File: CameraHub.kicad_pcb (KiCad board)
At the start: 4 copper layers, 90.2 x 95.9 mm, 121 parts, among them J1 200528-0100, J10 TE_282834-4, J2 Header 01x04 0.1", J3 Header 01x04 0.1", J4 USB_C_Receptacle_USB2.0_16P, J5 USB_C_Receptacle_USB2.0_16P, J6 Header 01x04 0.1", J7 USB_C_Receptacle_USB2.0_16P, J8 USB_C_Receptacle_USB2.0_16P, J9 Header 01x04 0.1", U1 USBLC6-2P6, U10 USB2514B-I/M2, U11 MIC2026-1xM, U12 MIC2026-1xM, U14 TLV76733QWDRBxQ1, U2 USBLC6-2P6, U3 USBLC6-2P6, U4 USB2514B-I/M2, U5 MIC2026-1xM, U6 MIC2026-1xM, U7 USBLC6-2P6, U8 USBLC6-2P6, U9 USBLC6-2P6, Y1 24MHz, Y2 24MHz

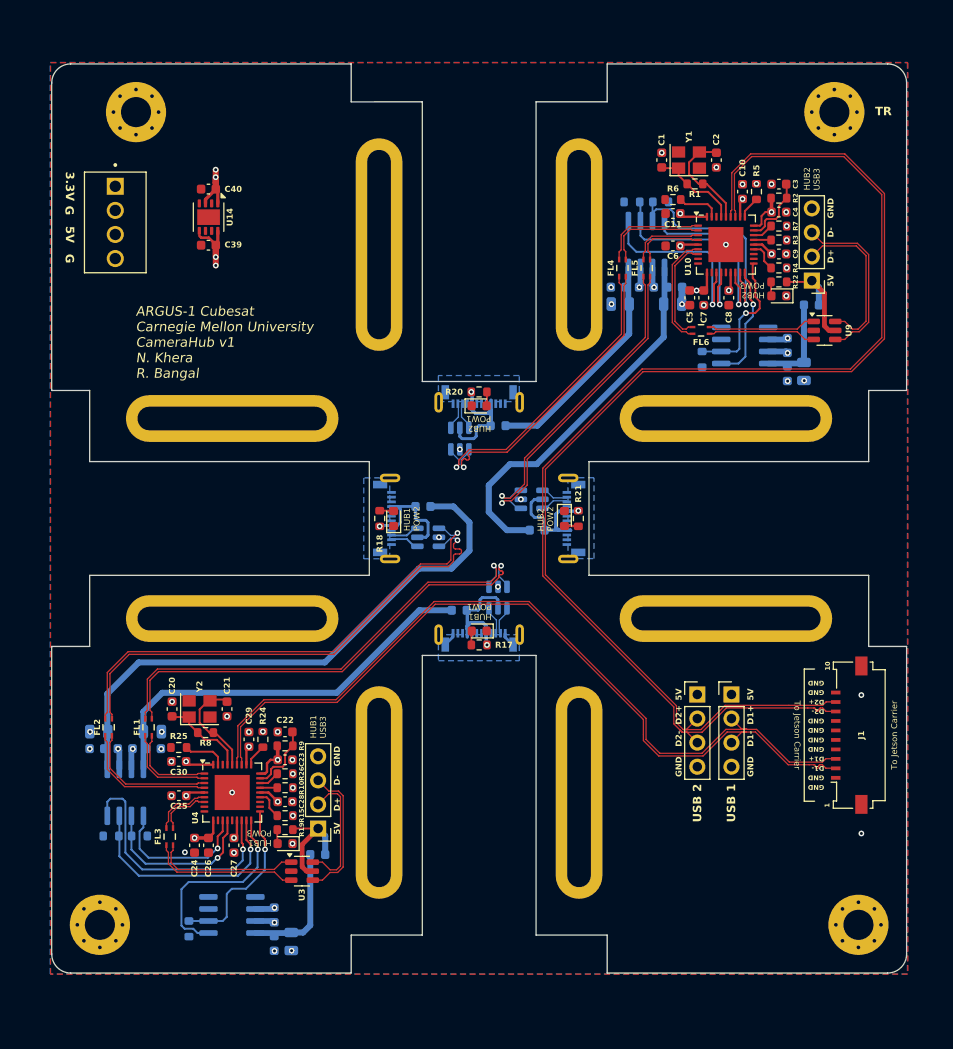
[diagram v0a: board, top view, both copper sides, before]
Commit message: Updated for single USB line
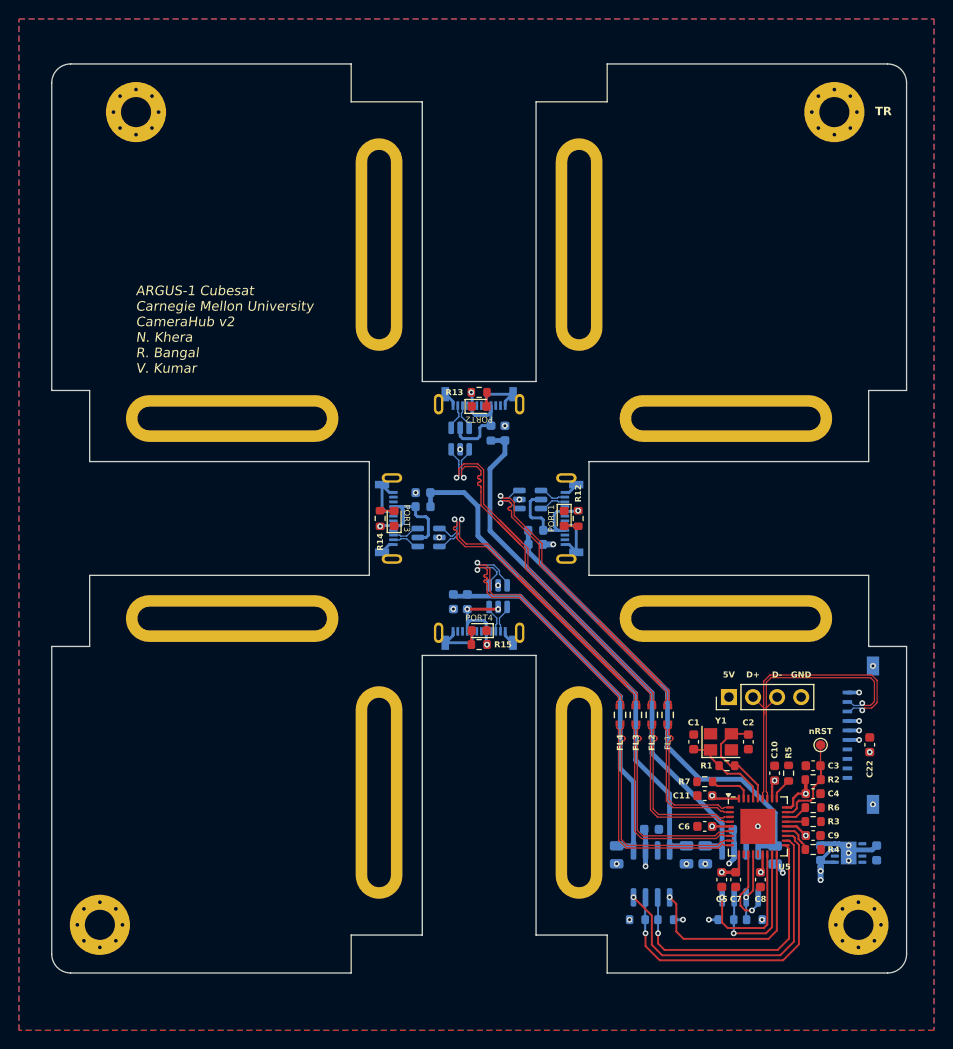
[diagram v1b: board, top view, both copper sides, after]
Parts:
- removed the C20 at (116.5, 116.9)
- removed the C21 at (122.3, 116.9)
- removed the C23 at (128.4, 122.3)
- removed the C24 at (118.9, 131.3)
- removed C25, C26, C27, C28, C29, C30, C31, C33, C35, C36, C38: 0.1uF, Capacitor_SMD:C_0603_1608Metric
- removed C32, C34, C37: 100uF, Capacitor_SMD:C_0805_2012Metric
- removed the D1 at (148.9, 108.7)
- removed the D2 at (139.9, 96.8)
- removed the D3 at (128.4, 131.1)
- removed the FB1 at (146.8, 106.5)
- removed FB6: 600R, Inductor_SMD:L_0603_1608Metric
- removed FL5, FL6: 744230900, CameraHub:CHIP_230900_WRE
- removed the J1 at (187.4, 119.7)
- removed J10: TE_282834-4, CameraHub:TE_282834-4
- removed the J2 at (175.5, 115.4)
- removed the J5 at (139.7, 96.8)
- removed J9: Header 01x04 0.1", Connector_PinHeader_2.54mm:PinHeader_1x04_P2.54mm_Vertical
- removed the R10 at (128.4, 125.2)
- removed R17, R18, R19: 330R, Resistor_SMD:R_0603_1608Metric
- removed R24, R26: 36K, Resistor_SMD:R_0603_1608Metric
- removed R25: 12K, Resistor_SMD:R_0603_1608Metric
- removed R30, R31, R33: 10K, Resistor_SMD:R_0603_1608Metric
- removed the R8 at (120.0, 119.4)
- removed the R9 at (128.4, 120.8)
- removed the U1 at (150.9, 105.2)
- removed the U2 at (143.5, 98.8)
- removed the U3 at (130.2, 134.0)
- removed the U5 at (111.6, 125.7)
- removed the U6 at (122.8, 138.7)
- removed Y2: 24MHz, Crystal:Crystal_SMD_3225-4Pin_3.2x2.5mm
- added C18: 100uF, Capacitor_SMD:C_0805_2012Metric, B.Cu at (163.4, 132.3)
- added C19: 0.1uF, Capacitor_SMD:C_0603_1608Metric, B.Cu at (146.2, 105.6)
- added D4: Green, LED_SMD:LED_0603_1608Metric, F.Cu at (148.9, 108.7)
- added J3: USB_C_Receptacle_USB2.0_16P, CameraHub:USBC-121SMT-4BS2S, B.Cu at (139.9, 96.8)
- added R11: 10K, Resistor_SMD:R_0603_1608Metric, B.Cu at (165.6, 139.1)
- added nRST: Conn_01x01, TestPoint:TestPoint_Pad_D1.0mm, F.Cu at (184.9, 120.7)
- C22: value 0.1uF -> 1uF
- C23: renamed from C39; moved to B.Cu
- C24: renamed from C40; moved to B.Cu
- J6: value Header 01x04 0.1" -> 200528-0100; footprint Connector_PinHeader_2.54mm:PinHeader_1x04_P2.54mm_Vertical -> Connector_FFC-FPC:Molex_200528-0100_1x10-1MP_P1.00mm_Horizontal; moved to B.Cu
- R15: value 36K -> 330R
- U3: renamed from U9; moved to B.Cu
- U4: value USB2514B-I/M2 -> USBLC6-2P6; footprint Package_DFN_QFN:QFN-36-1EP_6x6mm_P0.5mm_EP3.7x3.7mm -> Package_TO_SOT_SMD:SOT-23-6; moved to B.Cu
- U8: renamed from U14; moved to B.Cu
- moved C23 95.3 mm to (190.8, 132.1), turned to 90 degrees
- moved C24 95.2 mm to (184.9, 132.1), turned to 90 degrees
- moved U8 95.2 mm to (187.9, 132.1), turned to 0 degrees
- moved R8 76.8 mm to (177.9, 139.1), turned to 180 degrees
- moved R9 76.0 mm to (174.9, 139.1), turned to 0 degrees
- moved U6 67.1 mm to (176.4, 134.3), turned to 90 degrees
- moved C22 61.7 mm to (190.1, 120.7), turned to -90 degrees
- moved R7 61.5 mm to (172.7, 124.6)
- moved C11 61.5 mm to (172.7, 126.1)
- moved U5 61.5 mm to (178.3, 129.3)
- moved C1 61.5 mm to (171.5, 120.4)
- moved C2 61.5 mm to (177.3, 120.4)
- moved C5 61.5 mm to (174.5, 134.9)
- moved C7 61.5 mm to (176.0, 134.9)
- moved R1 61.5 mm to (175.0, 122.9)
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- renumbered C18 to C20, C19 to C21, D4 to D1, D5 to D2, D6 to D3, FB2 to FB1, FB5 to FB2, J7 to J1, J8 to J2, J3 to J5, R16 to R10, R20 to R12, R21 to R13, R22 to R14, R7 to R6, R6 to R7, R11 to R8, R12 to R9, U7 to U1, U8 to U2, U10 to U5, U11 to U6, U12 to U7
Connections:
- net /nRST2 renamed /nRST
- C22 pad 1: /nRST1 -> GND
- C22 pad 2: GND -> +5V
- FB3 pad 1: /Hub 1/VBUS3 -> /Hub 2/VBUS3
- FB3 pad 2: /Hub 1/VBUS_CONN3 -> /Hub 2/VBUS_CONN3
- FB4 pad 1: /Hub 1/VBUS2 -> /Hub 2/VBUS4
- FB4 pad 2: /Hub 1/VBUS_CONN2 -> /Hub 2/VBUS_CONN4
- FL1 pad 1: /Hub 1/HD1_P -> /Hub 2/HD1_P
- FL1 pad 2: /Hub 1/FD1_P -> /Hub 2/FD1_P
- FL1 pad 3: /Hub 1/FD1_N -> /Hub 2/FD1_N
- FL1 pad 4: /Hub 1/HD1_N -> /Hub 2/HD1_N
- FL2 pad 1: /Hub 1/HD2_P -> /Hub 2/HD2_P
- FL2 pad 2: /Hub 1/FD2_P -> /Hub 2/FD2_P
- FL2 pad 3: /Hub 1/FD2_N -> /Hub 2/FD2_N
- FL2 pad 4: /Hub 1/HD2_N -> /Hub 2/HD2_N
- FL3 pad 1: /Hub 1/HD3_P -> /Hub 2/HD3_P
- FL3 pad 2: /Hub 1/FD3_P -> /Hub 2/FD3_P
- FL3 pad 3: /Hub 1/FD3_N -> /Hub 2/FD3_N
- FL3 pad 4: /Hub 1/HD3_N -> /Hub 2/HD3_N
- FL4 pad 1: /Hub 2/HD1_P -> /Hub 2/HD4_P
- FL4 pad 2: /Hub 2/FD1_P -> /Hub 2/FD4_P
- FL4 pad 3: /Hub 2/FD1_N -> /Hub 2/FD4_N
- FL4 pad 4: /Hub 2/HD1_N -> /Hub 2/HD4_N
- J4 pad A4: /Hub 1/VBUS_CONN1 -> /Hub 2/VBUS_CONN4
- J4 pad A6: /Hub 1/D1_P -> /Hub 2/D4_P
- J4 pad A7: /Hub 1/D1_N -> /Hub 2/D4_N
- J4 pad B9: /Hub 1/VBUS_CONN1 -> /Hub 2/VBUS_CONN4
- J5 pad 2: /USB2_P -> /USB_P
- J5 pad 3: /USB2_N -> /USB_N
- J6 pad 1: /Hub 1/VBUS_CONN3 -> GND
- J6 pad 2: /Hub 1/D3_P -> /USB_N
- J6 pad 3: /Hub 1/D3_N -> /USB_P
- R15 pad 1: Net-(U4-SDA/SMBDATA/NON_REM1) -> /Hub 2/VBUS_CONN4
- R15 pad 2: GND -> Net-(D4-A)
- U4 pad 1: /Hub 1/HD1_N -> /Hub 2/FD4_P
- U4 pad 2: /Hub 1/HD1_P -> GND
- U4 pad 3: /Hub 1/HD2_N -> /Hub 2/FD4_N
- U4 pad 4: /Hub 1/HD2_P -> /Hub 2/D4_N
- U4 pad 5: +3.3V -> /Hub 2/VBUS_CONN4
- U4 pad 6: /Hub 1/HD3_N -> /Hub 2/D4_P
- U5 pad 20: unconnected-(U10-PRTPWR4/BC_EN4-Pad20) -> /Hub 2/PWR4
- U5 pad 21: unconnected-(U10-OCS_N4-Pad21) -> /Hub 2/nOCS4
- U5 pad 30: /USB2_N -> /USB_N
- U5 pad 31: /USB2_P -> /USB_P
- U5 pad 8: unconnected-(U10-USBDM_DN4/PRT_DIS_M4-Pad8) -> /Hub 2/HD4_N
- U5 pad 9: unconnected-(U10-USBDP_DN4/PRT_DIS_P4-Pad9) -> /Hub 2/HD4_P
- U7 pad 3: unconnected-(U12-FLGB-Pad3) -> /Hub 2/nOCS4
- U7 pad 4: unconnected-(U12-ENB-Pad4) -> /Hub 2/PWR4
- U7 pad 5: unconnected-(U12-OUTB-Pad5) -> /Hub 2/VBUS4
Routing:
- net /USB2_N: track 133.7 -> 0.00 mm
- net /USB2_P: track 132.7 -> 0.00 mm
- net /USB1_P: track 85.8 -> 0.00 mm
- net /USB1_N: track 85.6 -> 0.00 mm
- net /Hub 1/VBUS2: track 60.2 -> 0.00 mm
- net /Hub 2/FD3_N: track 11.4 -> 65.0 mm, vias 0 -> 1
- net /Hub 2/FD3_P: track 11.4 -> 65.0 mm, vias 0 -> 1
- net /Hub 1/FD2_N: track 52.0 -> 0.00 mm, vias 1 -> 0
- net /Hub 1/FD2_P: track 51.6 -> 0.00 mm, vias 1 -> 0
- net /Hub 1/FD1_N: track 49.7 -> 0.00 mm, vias 1 -> 0
- net /Hub 1/FD1_P: track 49.1 -> 0.00 mm, vias 1 -> 0
- net /Hub 2/VBUS3: track 9.88 -> 53.5 mm
- net /Hub 1/VBUS1: track 42.2 -> 0.00 mm
- net /Hub 2/VBUS4: track 0.00 -> 40.4 mm
- net /Hub 2/nOCS4: track 0.00 -> 35.1 mm, vias 0 -> 1
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- added copper zone on In2.Cu, net +3.3V
- added copper zone on B.Cu, net +5V
- removed copper zone on B.Cu, net +3.3V
- removed copper zone on In2.Cu, net +5V
- removed copper zone on B.Cu, net GND
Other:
- board text added: "ARGUS-1 Cubesat Carnegie Mellon University CameraHub v2 N. Khera R. Bangal V. Kumar"
- board text added: "JETSON CARRIER"
- board text added: "PORT1"
- board text added: "PORT2"
- board text added: "PORT3"
- board text added: "PORT4"
- board text added: "USB1"
- board text added: "USB2"
- board text added: "USB3"
- board text added: "USB4"
- board text removed: "3.3V"
- board text removed: "ARGUS-1 Cubesat Carnegie Mellon University CameraHub v1 N. Khera R. Bangal"
- board text removed: "D1+"
- board text removed: "D1-"
- board text removed: "D2+"
- board text removed: "D2-"
- board text removed: "G"
- board text removed: "HUB1 POW1"
- board text removed: "HUB1 POW2"
- board text removed: "HUB1 POW3"
- board text removed: "HUB1 USB1"
- board text removed: "HUB1 USB2"
- board text removed: "HUB1 USB3"
- board text removed: "HUB2 POW1"
- board text removed: "HUB2 POW2"
- board text removed: "HUB2 POW3"
- board text removed: "HUB2 USB1"
- board text removed: "HUB2 USB2"
- board text removed: "HUB2 USB3"
- board text removed: "USB 1"
- board text removed: "USB 2"
